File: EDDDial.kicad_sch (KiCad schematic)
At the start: 49 parts, among them J1 USB_C_Receptacle_USB2.0_16P, J2 Conn_01x03_MountingPin, J3 Conn_ARM_SWD_TagConnect_TC203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, J4 Conn_01x05_MountingPin, J5 Conn_01x05_MountingPin, U1 nRF52820-QDxx, U3 WE-TVS-82400102, U4 TPS7A02DBV, U5 TMAG5173A1QDBVRQ1, U6 BQ24072RGT, Y1 32mhz, Y2 32.768khz

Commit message: primary design done, may change some minor things
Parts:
- removed C12, C15: 4.7uF, Capacitor_SMD:C_0402_1005Metric, symbol Device:C
- removed C14, C16, C18: 100nF, Capacitor_SMD:C_0402_1005Metric, symbol Device:C
- removed C17, C20: 1uF, Capacitor_SMD:C_0402_1005Metric, symbol Device:C
- removed C19: 100pF, Capacitor_SMD:C_0402_1005Metric, symbol Device:C
- removed C21: 47nF, Capacitor_SMD:C_0402_1005Metric, symbol Device:C
- removed C22: 1pF, Capacitor_SMD:C_0402_1005Metric, symbol Device:C
- removed C23: 1.2pF, Capacitor_SMD:C_0402_1005Metric, symbol Device:C
- removed D1: LED, LED_SMD:LED_0402_1005Metric, symbol Device:LED
- removed L1: 10uH, Inductor_SMD:L_0402_1005Metric, symbol Device:L_Small
- removed L2: 15nH, Inductor_SMD:L_0402_1005Metric, symbol Device:L_Small
- removed L3: 4.7nF, Inductor_SMD:L_0402_1005Metric, symbol Device:L_Small
- removed L4: 2.2nF, Inductor_SMD:L_0402_1005Metric, symbol Device:L_Small
- removed U1: nRF52820-QDxx, Package_DFN_QFN:QFN-40-1EP_5x5mm_P0.4mm_EP3.6x3.6mm, symbol MCU_Nordic:nRF52820-QDxx
- removed Y1: 32mhz, Crystal:Crystal_SMD_2012-2Pin_2.0x1.2mm, symbol Device:Crystal_Small
- added D2, D3: LED, LED_SMD:LED_0402_1005Metric, symbol Device:LED
- added R11, R14: 56k, Resistor_SMD:R_0402_1005Metric, symbol Device:R
- added R12: 100k, Resistor_SMD:R_0402_1005Metric, symbol Device:R
- added R13, R8: 4.7k, Resistor_SMD:R_0402_1005Metric, symbol Device:R
- added SW1: SW_SPDT, symbol Switch:SW_SPDT
- added SW2: SW_Push, symbol Switch:SW_Push
- added U2: MDBT50Q-1MV2, RF_Module:Raytac_MDBT50Q, symbol RF_Module:MDBT50Q-1MV2
- C13: value 4.7uF -> 10uF
- C4: value 12pF -> 10uF
- C6: value 12pF -> 0.1uF
- C9: value 820pF -> 0.1uF
- R3: value 1.5k -> 10k
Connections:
- net +3V3: now also C4.1, C6.1, C9.1, R14.1, U2.28 (VDD), U2.30 (VDDH)
- net GND: now also C4.2, C6.2, C9.2, D2.1 (K), D3.1 (K), R12.2, SW2.2, U2.1 (GND), U2.15 (GND), U2.2 (GND), U2.33 (GND), U2.55 (GND); no longer C4.1, C6.1, C9.1
- net INT: now also U2.19 (P0.26)
- net NRST: now also U2.40 (P0.18)
- net SCL: now also U2.27 (P0.11)
- net SDA: now also U2.29 (P0.12)
- net SWCLK: now also U2.53 (SWDCLK)
- net SWDIO: now also U2.51 (SWDIO)
- net USB_D+: now also U2.35 (D+)
- net USB_D-: now also U2.34 (D-)
- net VBAT: now also R11.1
- net VBUS: now also U2.32 (VBUS)
- net at C2.1, C3.1, U4.1 (VIN)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: now also SW1.1 (A); no longer R3.1, U6.10 (OUT), U6.11 (OUT)
- net SWO: now reaches J3.6 (SWO)
- net SWO: now also U2.47 (P1.00)
- net CHG: now reaches U6.9 (~{CHG})
- net CHG: now also R3.2, U2.16 (P0.27)
- net at C8.2, Y2.1: now also U2.17 (P0.00)
- net at C7.2, Y2.2: now also U2.18 (P0.01)
- new net: R13.2, U2.3 (P1.10)
- new net: R8.2, U2.8 (P1.15)
- new net: D2.2 (A), R8.1
- new net: D3.2 (A), R13.1
- new net: R3.1, SW1.2 (B), U6.10 (OUT), U6.11 (OUT)
- new net SWITCH: R14.2, SW2.1, U2.50 (P1.02)
- new net VDIV: R11.2, R12.1, U2.10 (P0.29)
- no-connect marks 3 -> 2
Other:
- moved on the sheet: C13, C2, C5, C7, C8, J5, R3, R4, R5, Y2

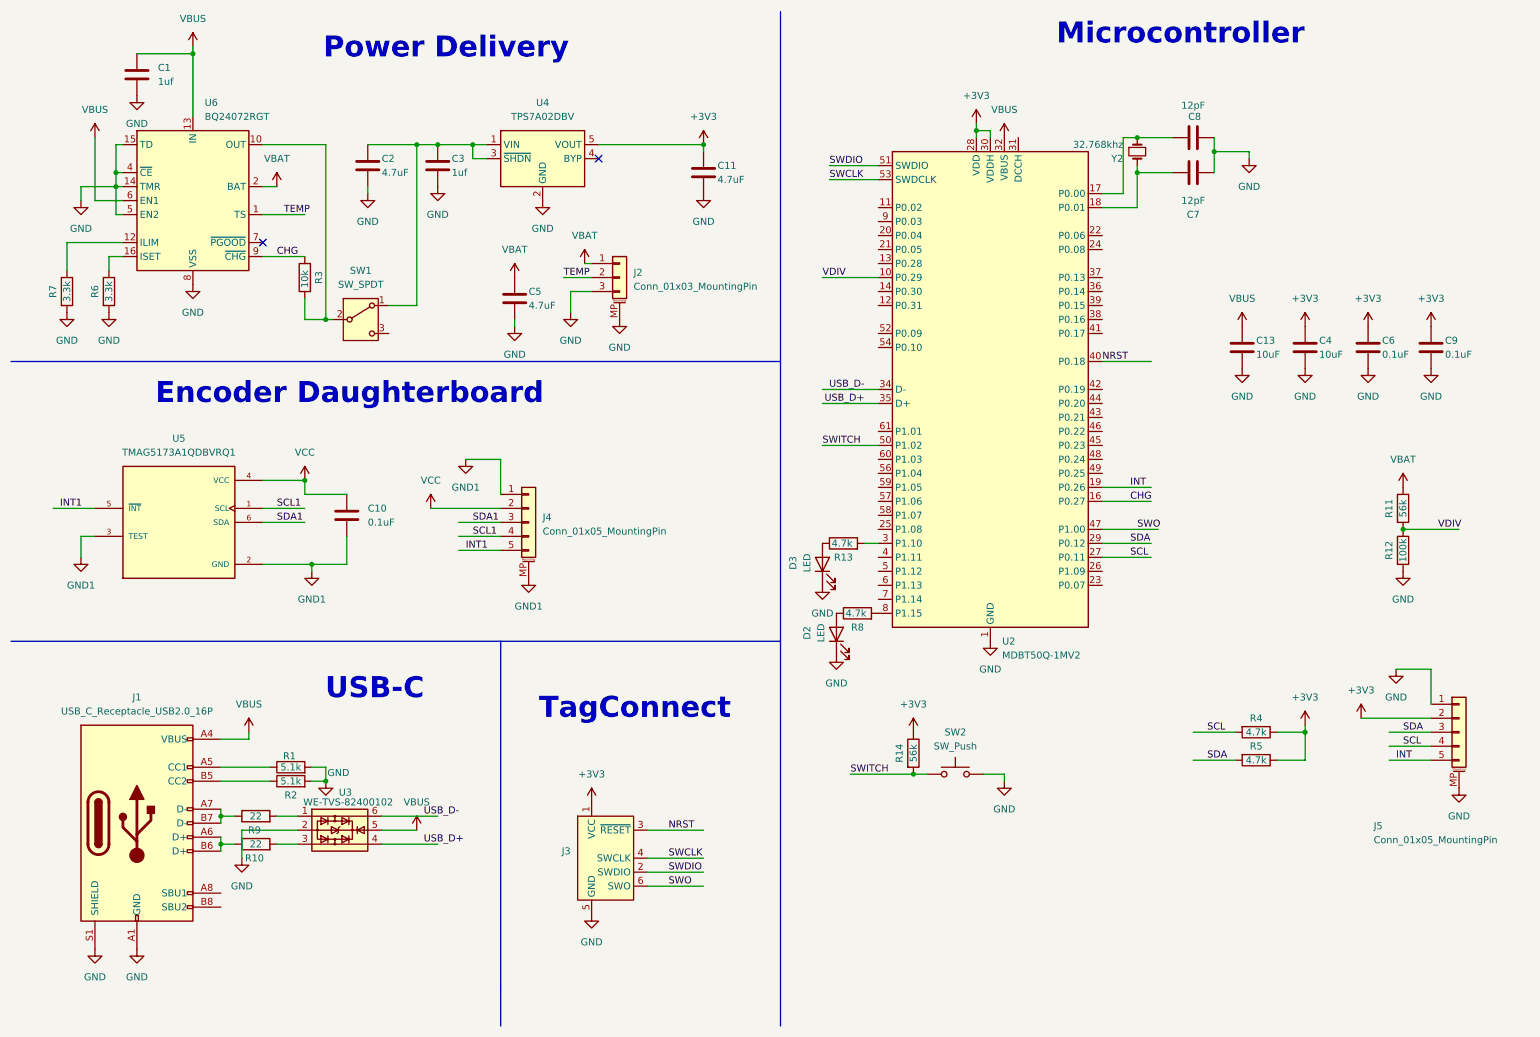
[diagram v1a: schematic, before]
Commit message: Updated to be 60mm dia and completed basic routing
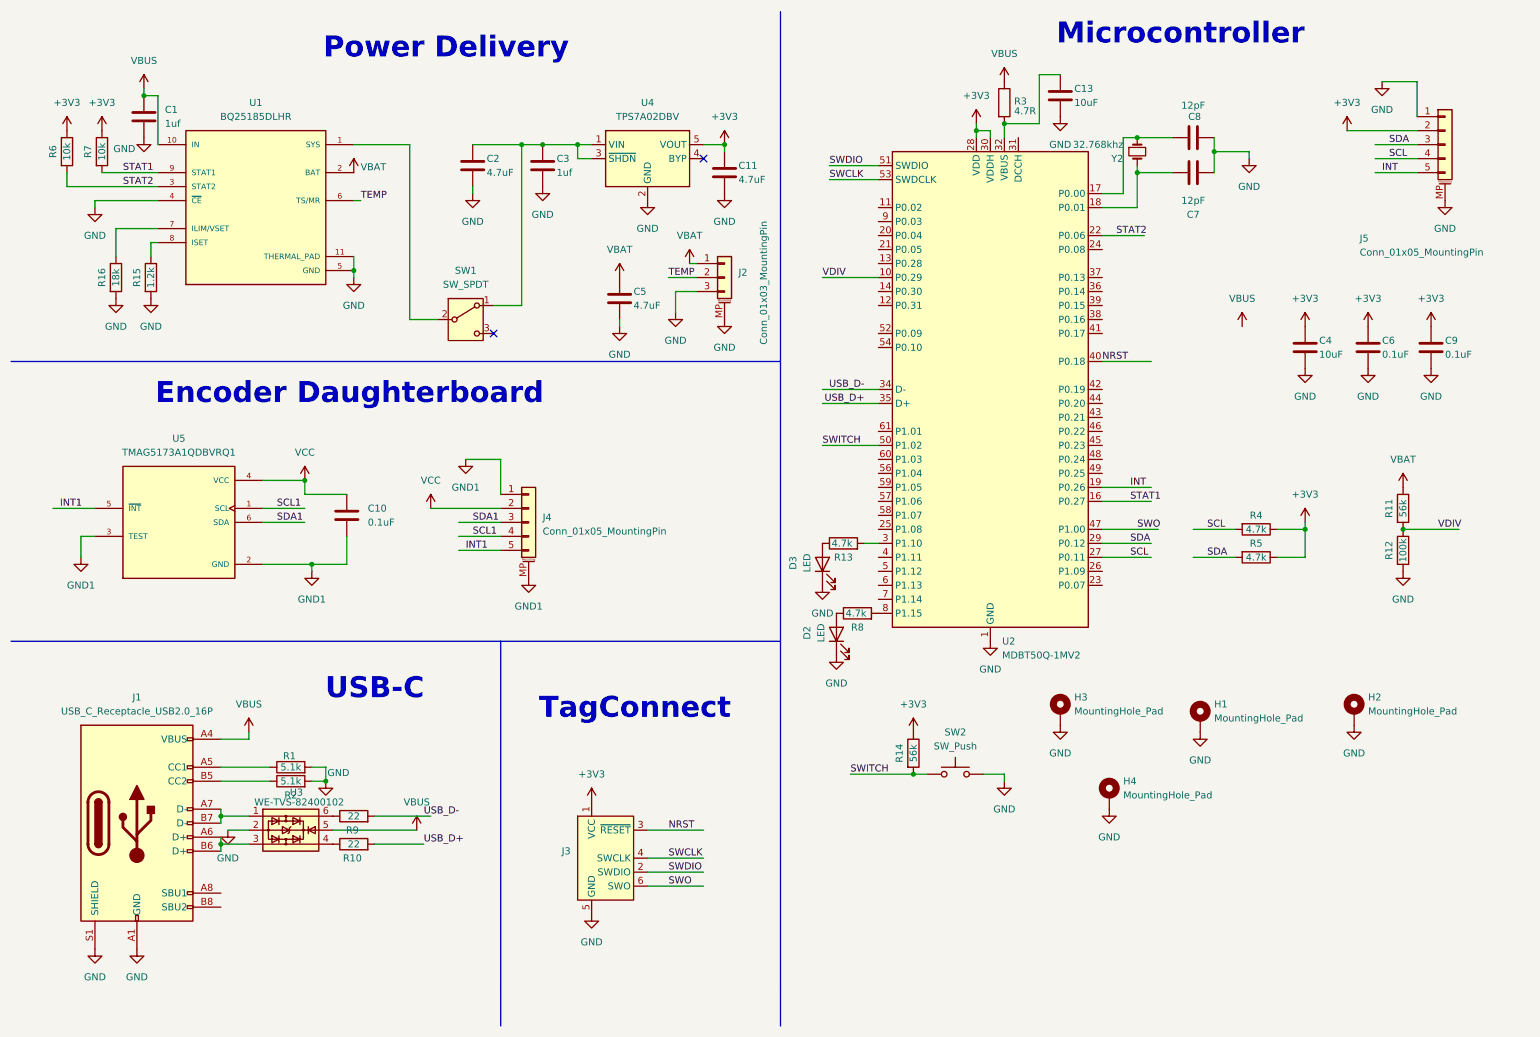
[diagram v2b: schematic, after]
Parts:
- removed U6: BQ24072RGT, Package_DFN_QFN:VQFN-16-1EP_3x3mm_P0.5mm_EP1.6x1.6mm, symbol Battery_Management:BQ24072RGT
- added H1, H2, H3, H4: MountingHole_Pad, MountingHole:MountingHole_2.2mm_M2_DIN965_Pad, symbol Mechanical:MountingHole_Pad
- added R15: 1.2k, Resistor_SMD:R_0402_1005Metric, symbol Device:R
- added R16: 18k, Resistor_SMD:R_0402_1005Metric, symbol Device:R
- added U1: BQ25185DLHR, FCU2025Lib:IC_BQ25185DLHR, symbol FCU2025:BQ25185DLHR
- R3: value 10k -> 4.7R; footprint Resistor_SMD:R_0402_1005Metric -> Resistor_SMD:R_0805_2012Metric
- R6, R7: value 3.3k -> 10k
- SW1: footprint (none) -> Button_Switch_THT:SW_E-Switch_EG1271_SPDT
- SW2: footprint (none) -> Button_Switch_SMD:SW_Push_1P1T_NO_CK_KSC6xxG
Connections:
- net +3V3: now also R6.1, R7.1
- net GND: now also H1.1, H2.1, H3.1, H4.1, R15.2, R16.2, U1.11 (THERMAL_PAD), U1.4 (~{CE}), U1.5 (GND); no longer R6.2, R7.2
- net TEMP: now also U1.6 (TS/MR)
- net USB_D+: now also R10.2; no longer U3.4
- net USB_D-: now also R9.2; no longer U3.6
- net VBAT: now also U1.2 (BAT)
- net VBUS: now also R3.1, U1.10 (IN); no longer C13.1, U2.32 (VBUS)
- net STAT2: now reaches U2.22 (P0.06)
- net STAT2: now also R6.2, U1.3 (STAT2)
- net at C2.1, C3.1, SW1.1 (A)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: now also SW1.4 (C)
- net at J1.A7 (D-), J1.B7 (D-): now also U3.1; no longer R9.1
- net at SW1.2 (B): now also SW1.5 (4), U1.1 (SYS); no longer R3.1
- net at U3.3: now also J1.A6 (D+), J1.B6 (D+); no longer R10.2
- net at SW1.3 (C): now also SW1.6 (C)
- net CHG: no longer names the net of R3.2
- net CHG: now also C13.1, U2.32 (VBUS); no longer U2.16 (P0.27)
- new net: R16.1, U1.7 (ILIM/VSET)
- new net: R15.1, U1.8 (ISET)
- new net: R9.1, U3.6
- new net: R10.1, U3.4
- new net STAT1: R7.2, U1.9 (STAT1), U2.16 (P0.27)
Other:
- moved on the sheet: C1, C11, C13, C2, C3, C5, J2, J5, R10, R4, R5, R6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

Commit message: produced device
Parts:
- added H5, H6, H7: MountingHole_Pad, MountingHole:MountingHole_2.2mm_M2_DIN965_Pad, symbol Mechanical:MountingHole_Pad
- D2, D3: footprint LED_SMD:LED_0402_1005Metric -> LED_SMD:LED_0603_1608Metric
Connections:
- net GND1: now also H5.1, H6.1, H7.1
